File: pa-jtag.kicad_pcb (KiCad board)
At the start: 2 copper layers, 83.8 x 31.8 mm, 25 parts, among them J1 USB_B, J2 JTAG, J3 VCCIO, J4 VOUT, U1 FT232RL, U2 L78L33_TO92

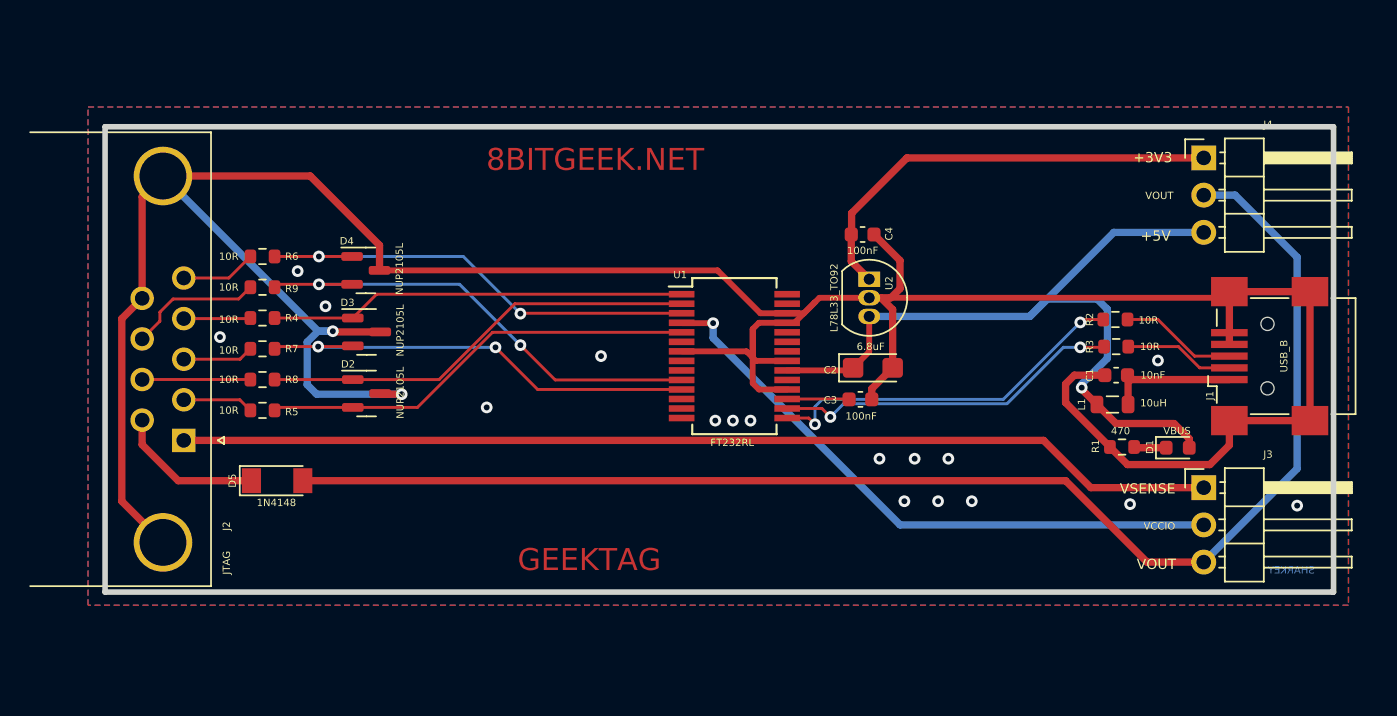
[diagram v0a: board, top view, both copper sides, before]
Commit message: Add J5 and Open Drain Resets
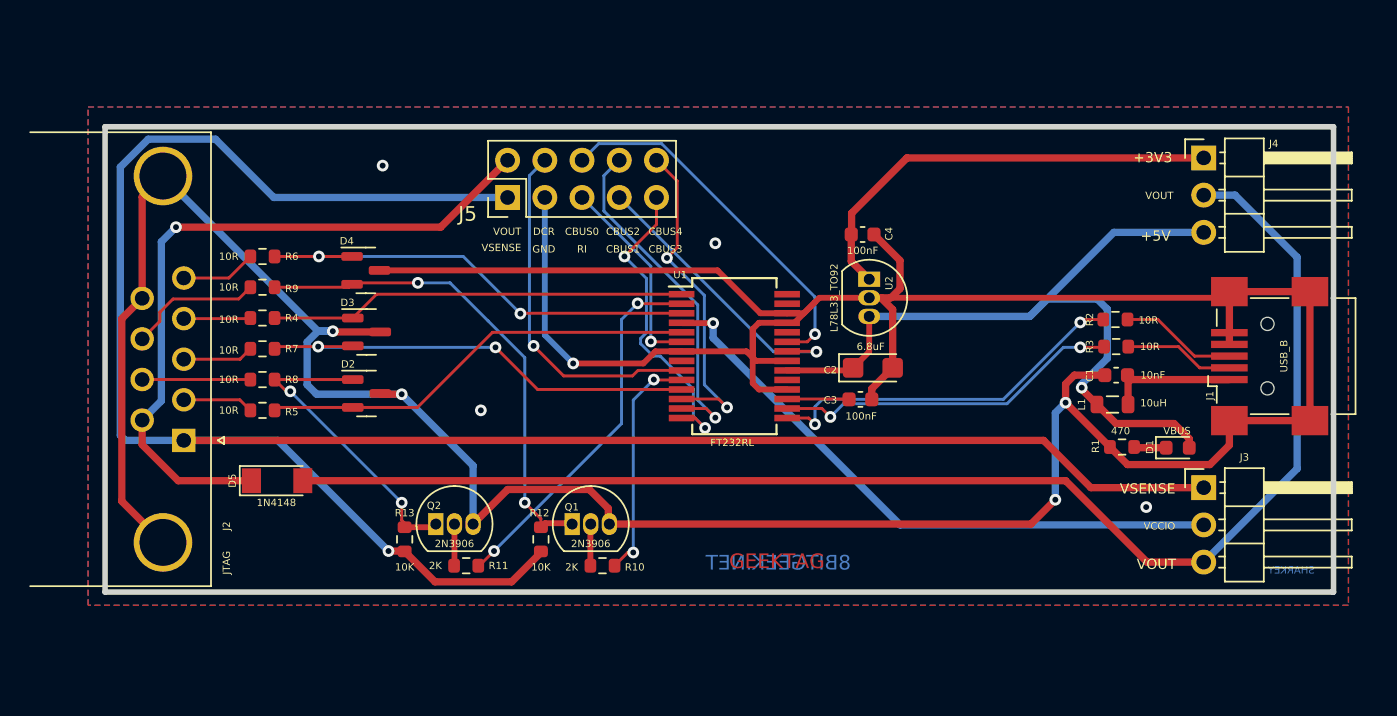
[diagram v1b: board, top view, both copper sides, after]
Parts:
- added J5: AUX, Connector_PinHeader_2.54mm:PinHeader_2x05_P2.54mm_Vertical, F.Cu at (146.6, 71.2)
- added Q1: 2N3906, Package_TO_SOT_THT:TO-92_Inline, F.Cu at (151.0, 93.5)
- added Q2: 2N3906, Package_TO_SOT_THT:TO-92_Inline, F.Cu at (141.7, 93.5)
- added R10: 2K, Resistor_SMD:R_0603_1608Metric, F.Cu at (153.1, 96.3)
- added R11: 2K, Resistor_SMD:R_0603_1608Metric, F.Cu at (143.8, 96.3)
- added R12: 10K, Resistor_SMD:R_0603_1608Metric, F.Cu at (148.9, 94.5)
- added R13: 10K, Resistor_SMD:R_0603_1608Metric, F.Cu at (139.6, 94.5)
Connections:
- U1 pad 10: Net-(R9-Pad2) -> Net-(U1-Pad10)
- U1 pad 12: unconnected-(U1-Pad12) -> /CBUS4
- U1 pad 13: unconnected-(U1-Pad13) -> /CBUS2
- U1 pad 14: unconnected-(U1-Pad14) -> /CBUS3
- U1 pad 2: Net-(R8-Pad2) -> Net-(U1-Pad2)
- U1 pad 22: unconnected-(U1-Pad22) -> /CBUS1
- U1 pad 23: unconnected-(U1-Pad23) -> /CBUS0
- U1 pad 6: unconnected-(U1-Pad6) -> /RI
- U1 pad 9: unconnected-(U1-Pad9) -> /DCR
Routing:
- net /VSENSE: track 70.9 -> 151.8 mm, vias 0 -> 1
- net GND: track 216.8 -> 279.0 mm, vias 19 -> 9
- net /VOUTR: track 10.2 -> 48.8 mm, vias 0 -> 1
- net Net-(U1-Pad2): track 0.00 -> 25.5 mm, vias 0 -> 2
- net /CBUS0: track 0.00 -> 25.4 mm, vias 0 -> 1
- net /DCR: track 0.00 -> 24.3 mm, vias 0 -> 1
- net /CBUS2: track 0.00 -> 23.7 mm, vias 0 -> 1
- net /CBUS4: track 0.00 -> 22.8 mm, vias 0 -> 2
- net /CBUS3: track 0.00 -> 21.4 mm, vias 0 -> 2
- net /CBUS1: track 0.00 -> 19.8 mm, vias 0 -> 1
- net Net-(U1-Pad10): track 0.00 -> 15.9 mm, vias 0 -> 2
- net /RI: track 0.00 -> 13.9 mm, vias 0 -> 1
- net Net-(R8-Pad2): track 29.9 -> 21.5 mm, vias 0 -> 2
- net Net-(Q2-Pad2): track 0.00 -> 2.85 mm
- net Net-(Q1-Pad2): track 0.00 -> 2.85 mm
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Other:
- board text added: "CBUS0"
- board text added: "CBUS1"
- board text added: "CBUS2"
- board text added: "CBUS3"
- board text added: "CBUS4"
- board text added: "DCR"
- board text added: "RI"

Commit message: ch32v103c schematic / placement
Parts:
- removed J3: VCCIO, Connector_PinHeader_2.54mm:PinHeader_1x03_P2.54mm_Horizontal
- removed Q1, Q2: 2N3906, Package_TO_SOT_THT:TO-92_Inline
- added C10: 20pF, Capacitor_SMD:C_0603_1608Metric, F.Cu at (165.5, 78.5)
- added C11: 100nF, Capacitor_SMD:C_0603_1608Metric, F.Cu at (173.5, 83.8)
- added C12: 100nF, Capacitor_SMD:C_0603_1608Metric, F.Cu at (176.2, 76.2)
- added C13: 100nF, Capacitor_SMD:C_0603_1608Metric, F.Cu at (186.8, 77.5)
- added C14: 100nF, Capacitor_SMD:C_0603_1608Metric, F.Cu at (174.2, 78.2)
- added C15: 100nF, Capacitor_SMD:C_0603_1608Metric, F.Cu at (146.2, 69.5)
- added C16: 6.8uF, Capacitor_Tantalum_SMD:CP_EIA-3216-18_Kemet-A, F.Cu at (188.5, 96.0)
- added C17: 100nF, Capacitor_SMD:C_0603_1608Metric, F.Cu at (184.2, 92.5)
- added C18: 100nF, Capacitor_SMD:C_0603_1608Metric, F.Cu at (132.0, 92.5)
- added C5: 100nF, Capacitor_SMD:C_0603_1608Metric, F.Cu at (132.0, 88.8)
- added C6: 100nF, Capacitor_SMD:C_0603_1608Metric, F.Cu at (138.5, 81.2)
- added C7: 100nF, Capacitor_SMD:C_0603_1608Metric, F.Cu at (144.2, 85.0)
- added C8: 20pF, Capacitor_SMD:C_0603_1608Metric, F.Cu at (165.5, 81.8)
- added C9: 100nF, Capacitor_SMD:C_0603_1608Metric, F.Cu at (132.0, 85.0)
- added D10: NUP2105L, Package_TO_SOT_SMD:SOT-23, F.Cu at (153.5, 88.0)
- added D11: NUP2105L, Package_TO_SOT_SMD:SOT-23, F.Cu at (162.0, 88.0)
- added D6: NUP2105L, Package_TO_SOT_SMD:SOT-23, F.Cu at (192.2, 76.5)
- added D7: 1N4148, Diode_SMD:D_MiniMELF, F.Cu at (192.8, 86.8)
- added D8: ST1, LED_SMD:LED_0603_1608Metric, F.Cu at (149.2, 95.8)
- added D9: ST0, LED_SMD:LED_0603_1608Metric, F.Cu at (165.0, 95.8)
- added J10: VCCIO, Connector_PinHeader_2.54mm:PinHeader_2x03_P2.54mm_Horizontal, F.Cu at (192.6, 91.5)
- added J7: SWD/SERIAL, Connector_PinHeader_2.54mm:PinHeader_2x06_P2.54mm_Horizontal, F.Cu at (180.3, 91.8)
- added J8: CH_SWD, Connector_PinHeader_2.54mm:PinHeader_1x06_P2.54mm_Vertical, F.Cu at (131.7, 76.5)
- added J9: JTAG, Connector_PinHeader_2.54mm:PinHeader_2x10_P2.54mm_Horizontal, F.Cu at (152.3, 72.4)
- added R14: 4K7, Resistor_SMD:R_0603_1608Metric, F.Cu at (190.0, 71.5)
- added R15: 4K7, Resistor_SMD:R_0603_1608Metric, F.Cu at (190.0, 69.5)
- added R16: 0R, Resistor_SMD:R_0603_1608Metric, F.Cu at (184.2, 90.8)
- added R17: 10K, Resistor_SMD:R_0603_1608Metric, F.Cu at (148.2, 69.5)
- added R18: 100R, Resistor_SMD:R_0603_1608Metric, F.Cu at (179.2, 89.2)
- added R19: 10K, Resistor_SMD:R_0603_1608Metric, F.Cu at (161.2, 84.0)
- added R20: 10K, Resistor_SMD:R_0603_1608Metric, F.Cu at (151.8, 84.0)
- added R21: 10K, Resistor_SMD:R_0603_1608Metric, F.Cu at (155.5, 84.0)
- added R22: 10K, Resistor_SMD:R_0603_1608Metric, F.Cu at (159.2, 84.0)
- added R23: 10R, Resistor_SMD:R_0603_1608Metric, F.Cu at (167.0, 88.0)
- added R24: 10R, Resistor_SMD:R_0603_1608Metric, F.Cu at (165.5, 88.0)
- added R25: 10R, Resistor_SMD:R_0603_1608Metric, F.Cu at (157.0, 88.2)
- added R26: 10R, Resistor_SMD:R_0603_1608Metric, F.Cu at (158.5, 88.2)
- added REF**: OSHW-Logo2_9.8x8mm_SilkScreen, Symbol:OSHW-Logo2_9.8x8mm_SilkScreen, F.Cu at (131.5, 70.8)
- added SW1: RESET, Button_Switch_SMD:SW_SPST_CK_RS282G05A3, F.Cu at (140.0, 70.2)
- added U3: CH32V103C8T6, Package_QFP:LQFP-48_7x7mm_P0.5mm, F.Cu at (181.2, 82.2)
- added Y1: 8M, Crystal:Crystal_HC49-4H_Vertical, F.Cu at (169.2, 82.7)
- J2: value JTAG -> RS232
- J5: footprint Connector_PinHeader_2.54mm:PinHeader_2x05_P2.54mm_Vertical -> Connector_PinHeader_2.54mm:PinHeader_2x05_P2.54mm_Horizontal
- R10, R11: value 2K -> 470
- U1: value FT232RL -> MAX3232; footprint Package_SO:SSOP-28_5.3x10.2mm_P0.65mm -> Package_SO:SOIC-16_3.9x9.9mm_P1.27mm
- moved D5 57.9 mm to (188.8, 91.2)
- moved R9 32.1 mm to (162.0, 76.2), turned to -90 degrees
- moved R6 30.4 mm to (160.2, 76.2), turned to -90 degrees
- moved R4 28.8 mm to (158.5, 76.2), turned to -90 degrees
- moved R7 27.4 mm to (156.8, 76.2), turned to -90 degrees
- moved R5 26.8 mm to (155.0, 76.2), turned to -90 degrees
- moved J5 25.8 mm to (162.0, 91.8), turned to -90 degrees
- moved U1 24.8 mm to (138.2, 88.8)
- moved R8 24.5 mm to (153.2, 76.2), turned to -90 degrees
- moved D4 23.7 mm to (160.2, 80.2), turned to -90 degrees
- moved R11 21.6 mm to (165.0, 92.2), turned to 90 degrees
- moved R13 20.8 mm to (157.5, 84.0)
- moved R1 20.8 mm to (190.0, 67.5)
- moved C2 20.5 mm to (186.8, 69.0), turned to 90 degrees
- moved D3 19.5 mm to (156.5, 80.2), turned to -90 degrees
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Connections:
- C2 pad 1: VBUS -> +5V
- C3 pad 1: Net-(C3-Pad1) -> +VSW
- C4 pad 1: /VREG -> +3V3
- D1 pad 2: VBUS -> +5V
- D2 pad 1: Net-(R8-Pad2) -> /MCU-TDI
- D2 pad 2: Net-(D2-Pad2) -> /MCU-TRST
- D3 pad 1: Net-(D3-Pad1) -> /MCU-TCK
- D3 pad 2: Net-(D3-Pad2) -> /MCU-TMS
- D4 pad 1: Net-(D4-Pad1) -> /MCU-SRST
- D4 pad 2: Net-(R9-Pad2) -> /MCU-TDO
- J1 pad 1: /VUSB -> Net-(D7-A)
- J2 pad 1: /VSENSE -> Net-(J2-Pad1)
- J2 pad 2: /TDI -> /TXD
- J2 pad 3: /TMS -> /RXD
- J2 pad 4: /TCK -> Net-(J2-Pad1)
- J2 pad 5: /TDO -> GND
- J2 pad 6: /VOUTR -> Net-(J2-Pad1)
- J2 pad 7: /TRST -> /CTS
- J2 pad 8: /SRST -> /RTS
- J2 pad 9: GND -> unconnected-(J2-Pad9)
- J4 pad 1: /VREG -> +3V3
- J4 pad 3: VBUS -> +5V
- J5 pad 1: /VSENSE -> +3V3
- J5 pad 10: /CBUS4 -> /AUX0
- J5 pad 2: /VOUTR -> +5V
- J5 pad 4: /DCR -> /AUX6
- J5 pad 5: /RI -> /AUX5
- J5 pad 6: /CBUS0 -> /AUX4
- J5 pad 7: /CBUS1 -> /AUX3
- J5 pad 8: /CBUS2 -> /AUX2
- J5 pad 9: /CBUS3 -> /AUX1
- L1 pad 2: VBUS -> +5V
- R10 pad 1: Net-(U1-Pad10) -> Net-(D8-K)
- R10 pad 2: Net-(Q1-Pad2) -> GND
- R11 pad 1: Net-(U1-Pad2) -> Net-(D9-K)
- R11 pad 2: Net-(Q2-Pad2) -> GND
- R12 pad 1: /VSENSE -> +VSW
- R12 pad 2: Net-(R9-Pad2) -> /MCU-TDI
- R13 pad 1: /VSENSE -> +VSW
- R13 pad 2: Net-(R8-Pad2) -> /MCU-TCK
- R2 pad 1: Net-(R2-Pad1) -> /UD+
- R3 pad 1: Net-(R3-Pad1) -> /UD-
- R4 pad 2: Net-(D3-Pad1) -> /MCU-TCK
- R5 pad 2: Net-(D2-Pad2) -> /MCU-TDI
- R6 pad 2: Net-(D4-Pad1) -> /MCU-TDO
- R7 pad 2: Net-(D3-Pad2) -> /MCU-TMS
- R8 pad 2: Net-(R8-Pad2) -> /MCU-TRST
- R9 pad 2: Net-(R9-Pad2) -> /MCU-SRST
- U1 pad 1: Net-(D3-Pad1) -> Net-(U1-C1+)
- U1 pad 10: Net-(U1-Pad10) -> /MCU_RS232_RTS
- U1 pad 11: Net-(D3-Pad2) -> /MCU_RS232_TX
- U1 pad 12: /CBUS4 -> /MCU_RS232_RX
- U1 pad 13: /CBUS2 -> /RXD
- U1 pad 14: /CBUS3 -> /TXD
- U1 pad 15: Net-(R2-Pad1) -> GND
- U1 pad 16: Net-(R3-Pad1) -> +VSW
- U1 pad 2: Net-(U1-Pad2) -> Net-(U1-VS+)
- U1 pad 3: Net-(D4-Pad1) -> Net-(U1-C1-)
- U1 pad 5: Net-(D2-Pad2) -> Net-(U1-C2-)
- U1 pad 6: /RI -> Net-(C18-Pad2)
- U1 pad 7: GND -> /RTS
- U1 pad 8: (no net) -> /CTS
- U1 pad 9: /DCR -> /MCU_RS232_CTS
- U2 pad 1: /VREG -> +3V3
- U2 pad 3: VBUS -> +5V
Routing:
- net GND: track 279.0 -> 0.00 mm, vias 9 -> 0
- net /VSENSE: track 151.8 -> 0.00 mm, vias 1 -> 0
- net /VOUT: track 95.4 -> 0.00 mm
- net VBUS: track 55.3 -> 0.00 mm, vias 1 -> 0
- net /VOUTR: track 48.8 -> 0.00 mm, vias 1 -> 0
- net Net-(U1-C2+): track 41.9 -> 0.00 mm, vias 1 -> 0
- net Net-(R9-Pad2): track 33.8 -> 0.00 mm, vias 2 -> 0
- net Net-(D4-Pad1): track 31.7 -> 0.00 mm, vias 2 -> 0
- net Net-(D3-Pad2): track 31.4 -> 0.00 mm, vias 2 -> 0
- net /VREG: track 30.6 -> 0.00 mm
- net Net-(D2-Pad2): track 30.0 -> 0.00 mm
- net Net-(D3-Pad1): track 28.4 -> 0.00 mm
- net Net-(U1-Pad2): track 25.5 -> 0.00 mm, vias 2 -> 0
- net Net-(R2-Pad1): track 25.4 -> 0.00 mm, vias 2 -> 0
- net /CBUS0: track 25.4 -> 0.00 mm, vias 1 -> 0
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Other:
- copper layers 2 -> 4
- board text added: "+VSW"
- board text added: "8bitgeek.net"
- board text added: "CTS"
- board text added: "RTS"
- board text added: "RXD"
- board text added: "TXD"
- board text added: "VSWD"
- board text removed: "8BITGEEK.NET"
- board text removed: "CBUS0"
- board text removed: "CBUS1"
- board text removed: "CBUS2"
- board text removed: "CBUS3"
- board text removed: "CBUS4"
- board text removed: "DCR"
- board text removed: "GEEKTAG"
- board text removed: "RI"
- board text removed: "SRST"
- board text removed: "TCK"
- board text removed: "TDI"
- board text removed: "TDO"
- board text removed: "TMS"
- board text removed: "TRST"
